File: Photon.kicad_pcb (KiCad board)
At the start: 4 copper layers, 21.3 x 95 mm, 50 parts, among them J1 USB_C_Receptacle_USB2.0_14P, SW1 TS-1088-AR02016, U1 ATtiny13A-S, U2 RT8059GJ5, U3 BQ24072RGTR, U4 BCR421UW6-7, U5 BCR421UW6-7

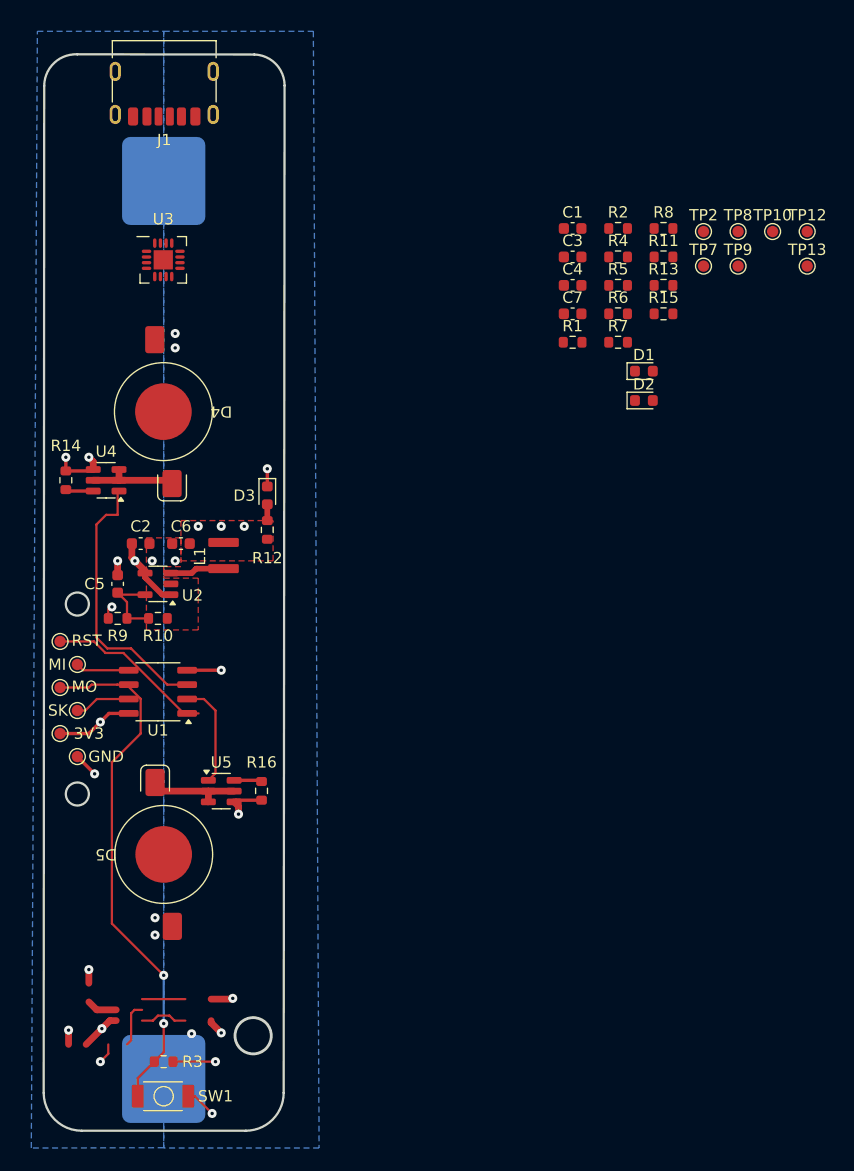
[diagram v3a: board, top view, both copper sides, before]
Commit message: Added TP4056 back
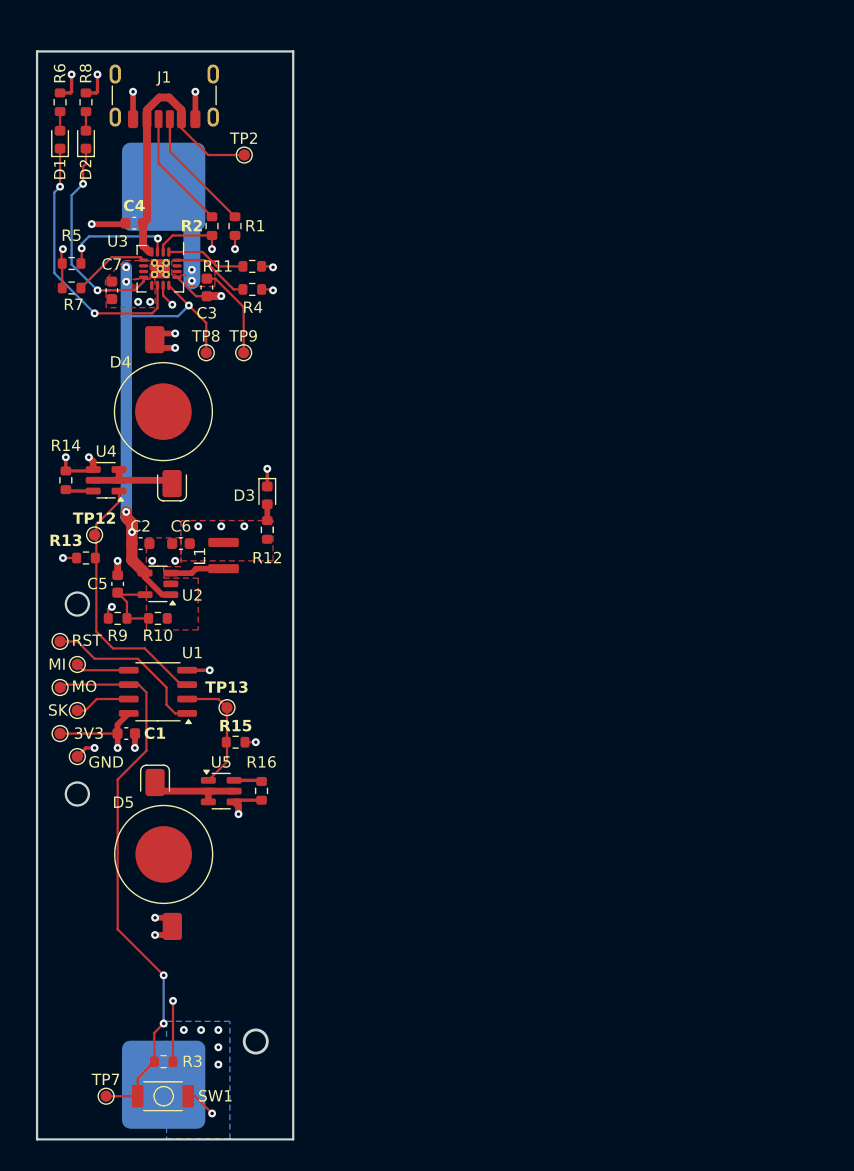
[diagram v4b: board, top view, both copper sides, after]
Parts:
- removed TP10: Vout, TestPoint:TestPoint_Pad_D1.0mm
- moved TP7 90.3 mm to (47.8, 112.3)
- moved TP12 68.3 mm to (46.7, 62.7)
- moved TP13 64.3 mm to (58.4, 78.0)
- moved C1 59.5 mm to (49.5, 80.3), turned to 180 degrees
- moved R13 56.4 mm to (46.0, 64.8), turned to 180 degrees
- moved D1 55.4 mm to (43.7, 27.9), turned to 90 degrees
- moved D2 54.4 mm to (46.0, 27.9), turned to 90 degrees
- moved R15 53.4 mm to (59.2, 81.0)
- moved R6 52.7 mm to (43.7, 24.6), turned to -90 degrees
- moved R8 52.2 mm to (46.0, 24.6), turned to -90 degrees
- moved R7 48.5 mm to (44.7, 40.9), turned to 180 degrees
- moved R5 48.3 mm to (44.7, 38.8), turned to 180 degrees
- moved TP8 48.1 mm to (56.6, 46.7)
- moved TP9 44.3 mm to (59.9, 46.7)
- moved TP2 41.1 mm to (59.9, 29.2)
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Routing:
- net VOUT: track 6.37 -> 51.4 mm, vias 1 -> 7
- net VCC: track 0.00 -> 25.0 mm
- net /PGOOD: track 0.00 -> 24.0 mm, vias 0 -> 2
- net /CHG: track 0.00 -> 18.8 mm, vias 0 -> 2
- net (no net): track 18.6 -> 0.00 mm, vias 3 -> 0
- net /BAT: track 0.00 -> 17.7 mm, vias 0 -> 2
- net GND: track 33.5 -> 48.7 mm, vias 13 -> 29
- net /3V6: track 13.0 -> 24.2 mm
- net /CC1: track 0.00 -> 11.0 mm
- net /CC2: track 0.00 -> 10.6 mm
- net /TMR: track 0.00 -> 10.0 mm, vias 0 -> 2
- net /ISET: track 0.00 -> 7.07 mm
- net /TS: track 0.00 -> 6.88 mm
- net /ILIM: track 0.00 -> 6.73 mm
- net /MISO_BTN: track 46.7 -> 50.1 mm
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- added copper zone on F.Cu, net /BAT
- added copper zone on F.Cu, net VOUT
- added copper zone on In2.Cu, net VOUT
- removed copper zone on B.Cu, net /BAT
- removed copper zone on In2.Cu, net VCC
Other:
- board size 21.3 x 95 mm -> 22.6 x 96 mm

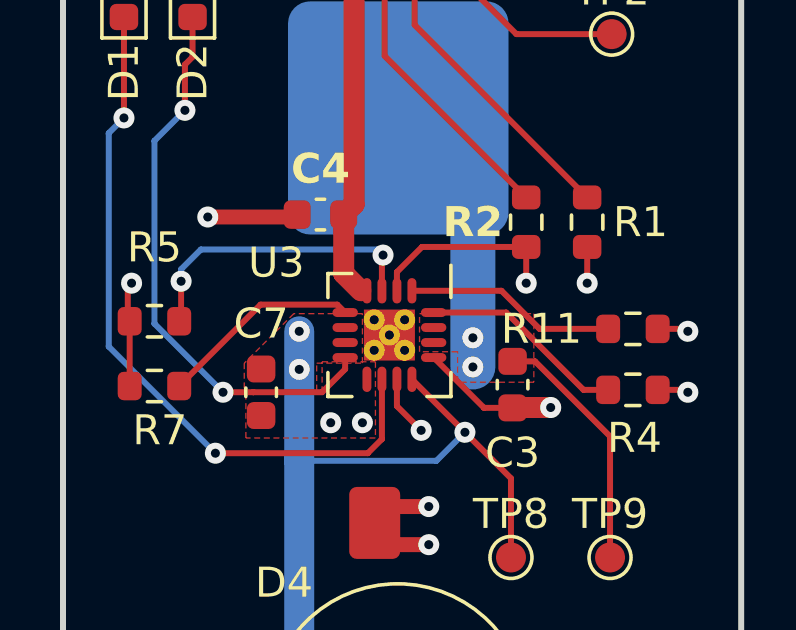
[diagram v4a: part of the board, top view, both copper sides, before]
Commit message: added usb detection circuit and battery protection
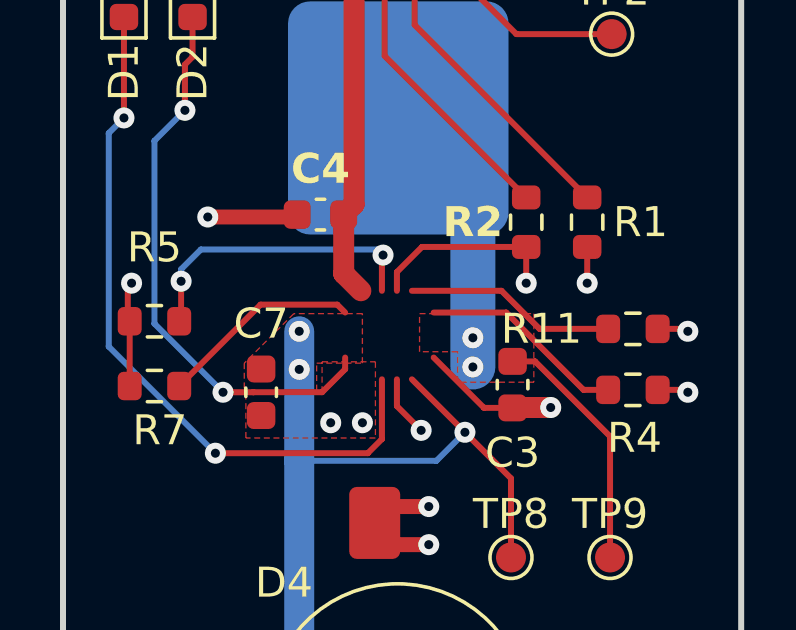
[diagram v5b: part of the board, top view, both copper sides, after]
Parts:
- removed U3: BQ24072RGTR, Photon:QFN-16_EP_3.8x3.8_Pitch0.5mm

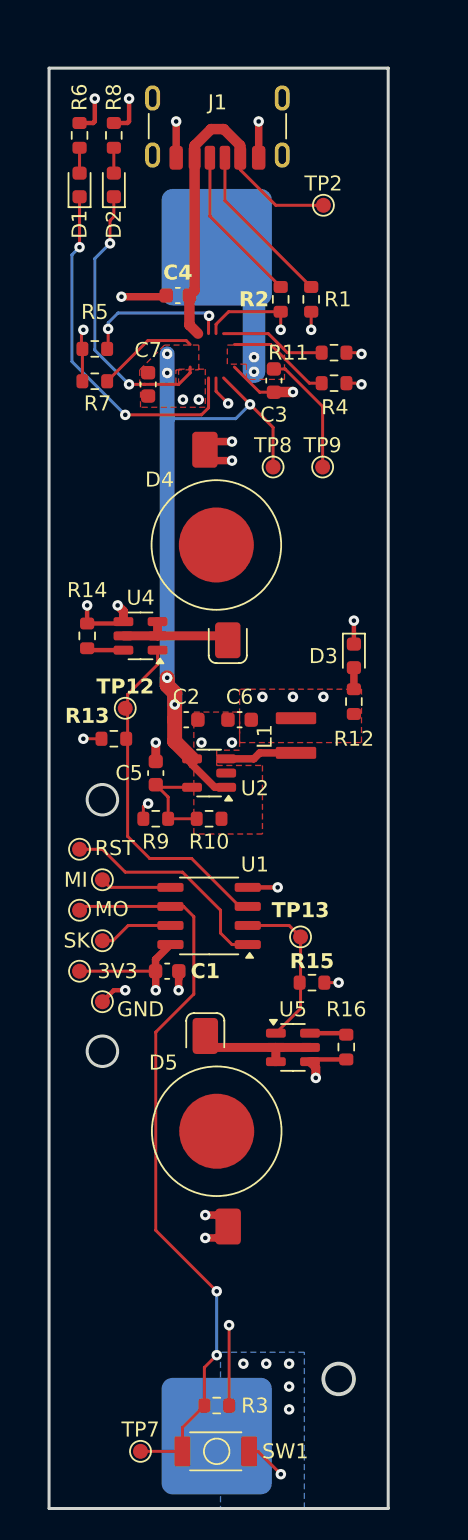
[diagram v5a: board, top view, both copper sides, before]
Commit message: PCB layout complete
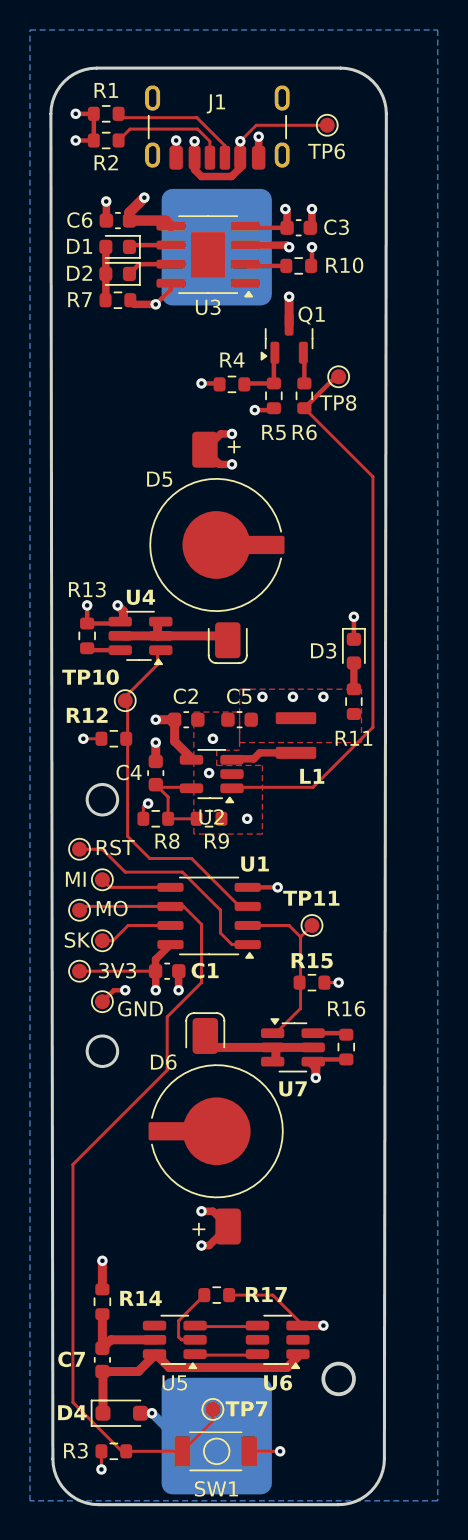
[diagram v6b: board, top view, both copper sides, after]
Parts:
- removed the C4 at (50.2, 35.2)
- removed the R11 at (60.7, 39.0)
- removed the R8 at (46.0, 24.6)
- removed the TP2 at (59.9, 29.2)
- removed the TP9 at (59.9, 46.7)
- added C6: 10uF, Capacitor_SMD:C_0603_1608Metric, F.Cu at (46.2, 30.2)
- added D4: D_Schottky, Diode_SMD:D_SOD-323_HandSoldering, F.Cu at (46.5, 109.7)
- added Q1: IRLML6402, Package_TO_SOT_SMD:SOT-23, F.Cu at (57.7, 38.1)
- added R10: 2K, Resistor_SMD:R_0603_1608Metric, F.Cu at (58.3, 33.2)
- added R14: 100R, Resistor_SMD:R_0603_1608Metric, F.Cu at (45.2, 102.3)
- added R17: 1K, Resistor_SMD:R_0603_1608Metric, F.Cu at (52.8, 101.9)
- added TP6: 5V, TestPoint:TestPoint_Pad_D1.0mm, F.Cu at (60.2, 23.9)
- added U3: TP4056, Package_SO:SOIC-8-1EP_3.9x4.9mm_P1.27mm_EP2.29x3mm, F.Cu at (52.3, 32.5)
- added U5: DW01A, Package_TO_SOT_SMD:SOT-23-6_Handsoldering, F.Cu at (50.0, 104.8)
- added U6: FS8205A, Package_TO_SOT_SMD:SOT-23-6_Handsoldering, F.Cu at (56.9, 104.8)
- C3: value 4.7uF -> 10uF
- C7: value 4.7uF -> 0.1uF
- R12: renamed from R13; value 10K -> 100K
- R15, R3: value 10K -> 100K
- R5: value 0R -> 100K
- R6: value 1K -> 0R
- R7: value 1.18K -> 2K
- R8: renamed from R9; value 500K -> 280K
- R9: renamed from R10; value 100K -> 62K
- U2: footprint Package_TO_SOT_SMD:SOT-23-5 -> Package_TO_SOT_SMD:SOT-23-5_HandSoldering
- U4: footprint Package_TO_SOT_SMD:SOT-23-6 -> Package_TO_SOT_SMD:SOT-23-6_Handsoldering
- U7: renamed from U5; footprint Package_TO_SOT_SMD:SOT-23-6 -> Package_TO_SOT_SMD:SOT-23-6_Handsoldering
- moved C7 65.1 mm to (45.2, 106.2)
- moved R6 22.9 mm to (58.7, 41.9), turned to 90 degrees
- moved R1 18.4 mm to (45.5, 23.1), turned to 180 degrees
- moved R2 15.7 mm to (45.5, 24.9), turned to 180 degrees
- moved R5 12.3 mm to (56.6, 41.9), turned to -90 degrees
- moved C3 10.3 mm to (58.3, 30.7), turned to 180 degrees
- moved R3 7.50 mm to (46.0, 112.3), turned to 0 degrees
- moved TP8 7.44 mm to (61.0, 40.6), turned to 90 degrees
- moved R4 6.80 mm to (53.8, 41.1), turned to 0 degrees
- moved D2 5.94 mm to (46.2, 33.8), turned to 180 degrees
- moved R7 5.62 mm to (46.2, 35.5)
- moved TP7 5.58 mm to (52.6, 109.5)
- moved D1 4.85 mm to (46.2, 32.0), turned to 180 degrees
- moved TP11 1.08 mm to (59.2, 77.2)
- moved TP10 0.51 mm to (46.7, 62.2)
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- renumbered C5 to C4, C6 to C5, D4 to D5, D5 to D6, R12 to R11, R14 to R13, TP12 to TP10, TP13 to TP11, TP4 to TP2, TP5 to TP4, TP6 to TP5, TP11 to TP9
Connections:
- net /3V6 renamed +3V3
- net Net-(D3-A) renamed /LED_A
- BT1 pad 1: /BAT -> PACK+
- BT1 pad 2: GND -> /Bat_Neg
- C2 pad 2: VOUT -> PACK+
- C3 pad 2: /BAT -> 5V
- C7 pad 1: GND -> /BAT_SAF_OUT
- C7 pad 2: VOUT -> /DW01A_VCC
- D1 pad 1: /PGOOD -> /STAT2
- D1 pad 2: /G_A -> /LED_PWR
- D2 pad 1: /CHG -> /STAT1
- D2 pad 2: /R_A -> /LED_PWR
- J1 pad A9: VCC -> 5V
- J1 pad B9: VCC -> 5V
- R4 pad 1: GND -> 5V
- R4 pad 2: /TS -> /PMOS_Gate
- R5 pad 1: /TMR -> /PMOS_Gate
- R6 pad 1: VOUT -> /BUCK_EN
- R6 pad 2: /G_A -> /PMOS_OUT
- R7 pad 1: /ILIM -> 5V
- R7 pad 2: GND -> /LED_PWR
- TP8 pad 1: VOUT -> /BUCK_EN
- U2 pad 1: VOUT -> /BUCK_EN
- U2 pad 4: VOUT -> PACK+
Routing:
- net VOUT: track 51.4 -> 0.00 mm, vias 7 -> 0
- net /BUCK_EN: track 0.00 -> 37.8 mm
- net VCC: track 25.0 -> 0.00 mm
- net /PGOOD: track 24.0 -> 0.00 mm, vias 2 -> 0
- net 5V: track 0.00 -> 22.4 mm, vias 0 -> 5
- net /CHG: track 18.8 -> 0.00 mm, vias 2 -> 0
- net /BAT: track 17.7 -> 0.00 mm, vias 2 -> 0
- net /BAT_SAF_OUT: track 0.00 -> 17.1 mm
- net PACK+: track 0.00 -> 13.0 mm, vias 0 -> 4
- net /TMR: track 10.0 -> 0.00 mm, vias 2 -> 0
- net /ISET: track 7.07 -> 0.00 mm
- net GND: track 48.7 -> 41.7 mm, vias 29 -> 23
- net /TS: track 6.88 -> 0.00 mm
- net /ILIM: track 6.73 -> 0.00 mm
- net /MISO_BTN: track 50.1 -> 56.4 mm, vias 2 -> 0
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- added copper zone on In2.Cu, net 5V
- added copper zone on B.Cu, net PACK+
- removed copper zone on F.Cu, net /BAT
- removed copper zone on B.Cu, net GND
- removed copper zone on F.Cu, net VOUT
- removed copper zone on In2.Cu, net VOUT
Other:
- board size 22.6 x 96 mm -> 22.4 x 95.8 mm

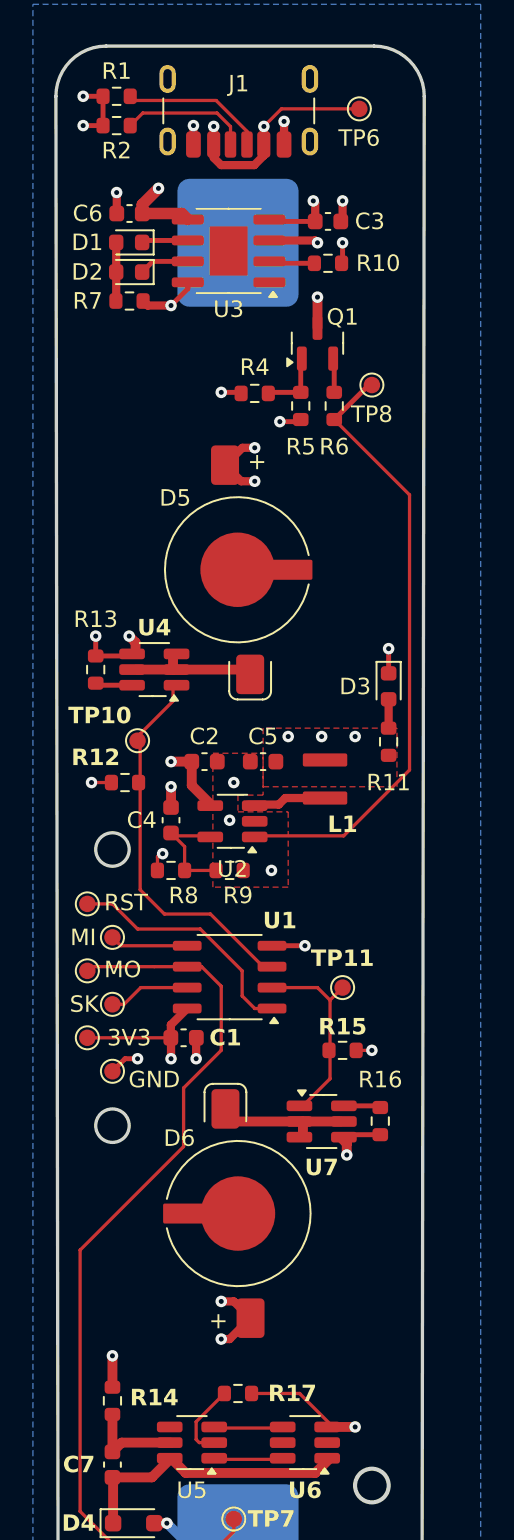
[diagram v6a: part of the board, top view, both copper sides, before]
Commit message: added fiducials and gerbers. - Ordered
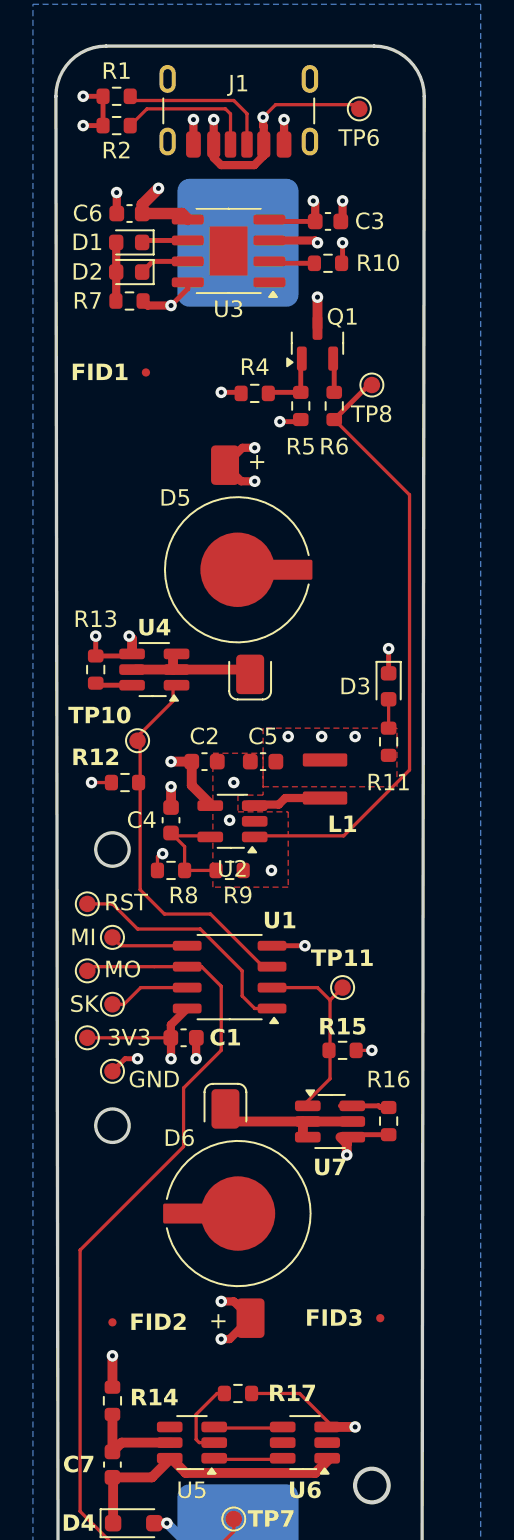
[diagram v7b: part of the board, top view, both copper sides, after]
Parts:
- added FID1: Fiducial, Fiducial:Fiducial_0.5mm_Mask1.5mm, F.Cu at (47.2, 39.9)
- added FID2: Fiducial, Fiducial:Fiducial_0.5mm_Mask1.5mm, F.Cu at (45.2, 97.5)
- added FID3: Fiducial, Fiducial:Fiducial_0.5mm_Mask1.5mm, F.Cu at (61.5, 97.3)
- moved U7 0.51 mm to (58.4, 85.3)
- moved R16 0.51 mm to (62.0, 85.3)
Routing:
- net 5V: track 22.4 -> 23.4 mm
- net GND: track 41.7 -> 42.4 mm
- net /CC2: track 7.83 -> 8.49 mm
- net /CC1: track 8.77 -> 9.40 mm
- net /Rext2: track 2.46 -> 2.97 mm

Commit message: updated gerbers
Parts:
- removed D4: D_Schottky, Diode_SMD:D_SOD-323_HandSoldering
- added Q2: IRLML6402, Package_TO_SOT_SMD:SOT-23, F.Cu at (48.3, 97.5)
- added R18: 10K, Resistor_SMD:R_0603_1608Metric, F.Cu at (54.9, 80.3)
- added R19: 100K, Resistor_SMD:R_0603_1608Metric, F.Cu at (49.3, 101.1)
- L1: value 4.7uH -> 2.2uH
- moved FID2 2.84 mm to (44.7, 94.7)
- moved FID3 2.79 mm to (61.5, 94.5)
- moved R14 1.06 mm to (46.2, 102.6)
- moved C7 1.05 mm to (46.2, 105.9)
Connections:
- BT1 pad 1: PACK+ -> /Bat+
- BT1 pad 2: /Bat_Neg -> /BAT_SAF_OUT
- R14 pad 1: PACK+ -> /Bat+
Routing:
- net /Bat+: track 0.00 -> 72.6 mm, vias 0 -> 1
- net /BAT_SAF_OUT: track 17.1 -> 28.0 mm, vias 0 -> 1
- net /Bat_Neg: track 5.88 -> 0.00 mm, vias 1 -> 0
- net +3V3: track 21.2 -> 23.5 mm, vias 11 -> 12
- net /RESET: track 14.7 -> 16.8 mm
- net Net-(Q2-G): track 0.00 -> 1.81 mm
- net /DW01A_VCC: track 6.06 -> 4.37 mm
- net /VM: track 5.01 -> 5.94 mm, vias 0 -> 2
